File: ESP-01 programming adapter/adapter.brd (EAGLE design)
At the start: 27 x 31 mm, 9 parts

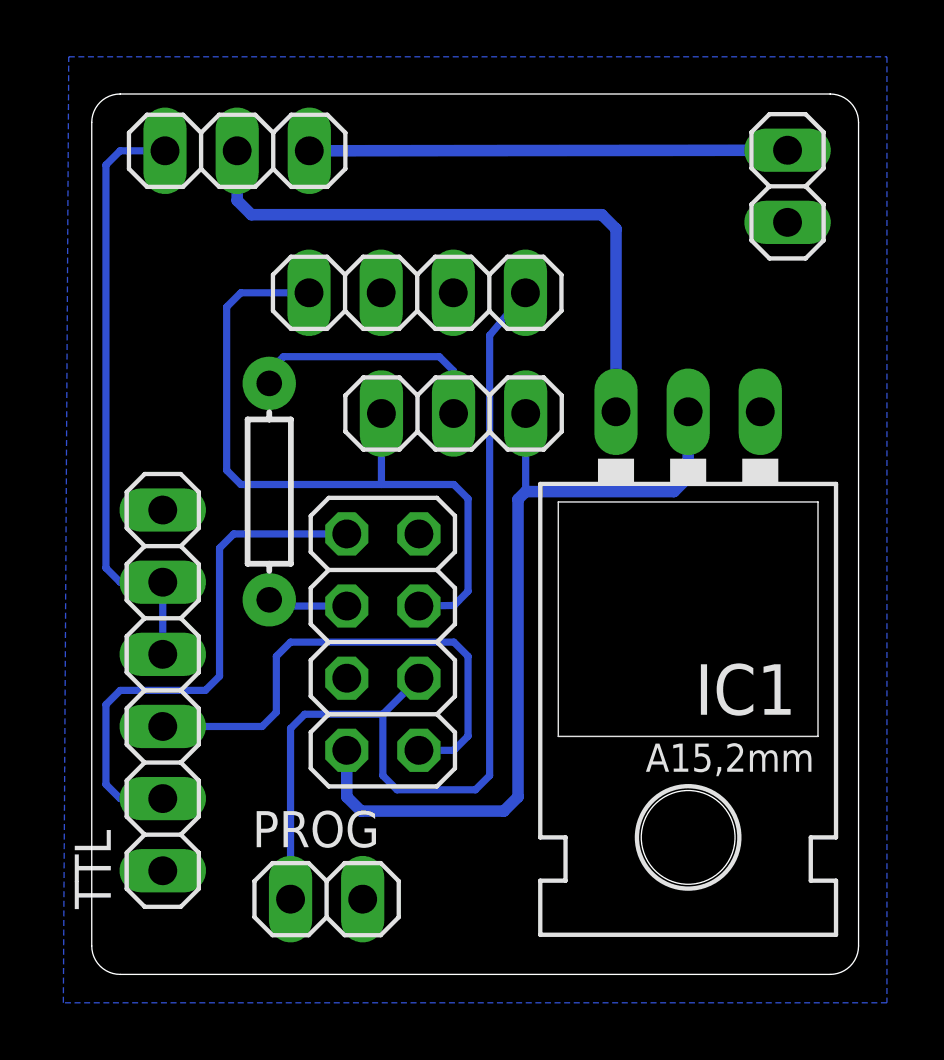
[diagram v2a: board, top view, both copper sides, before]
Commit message: CH_PD
Pin connected to GPIO00 instead of 02, so GPIO02 is free to do external
triggers.
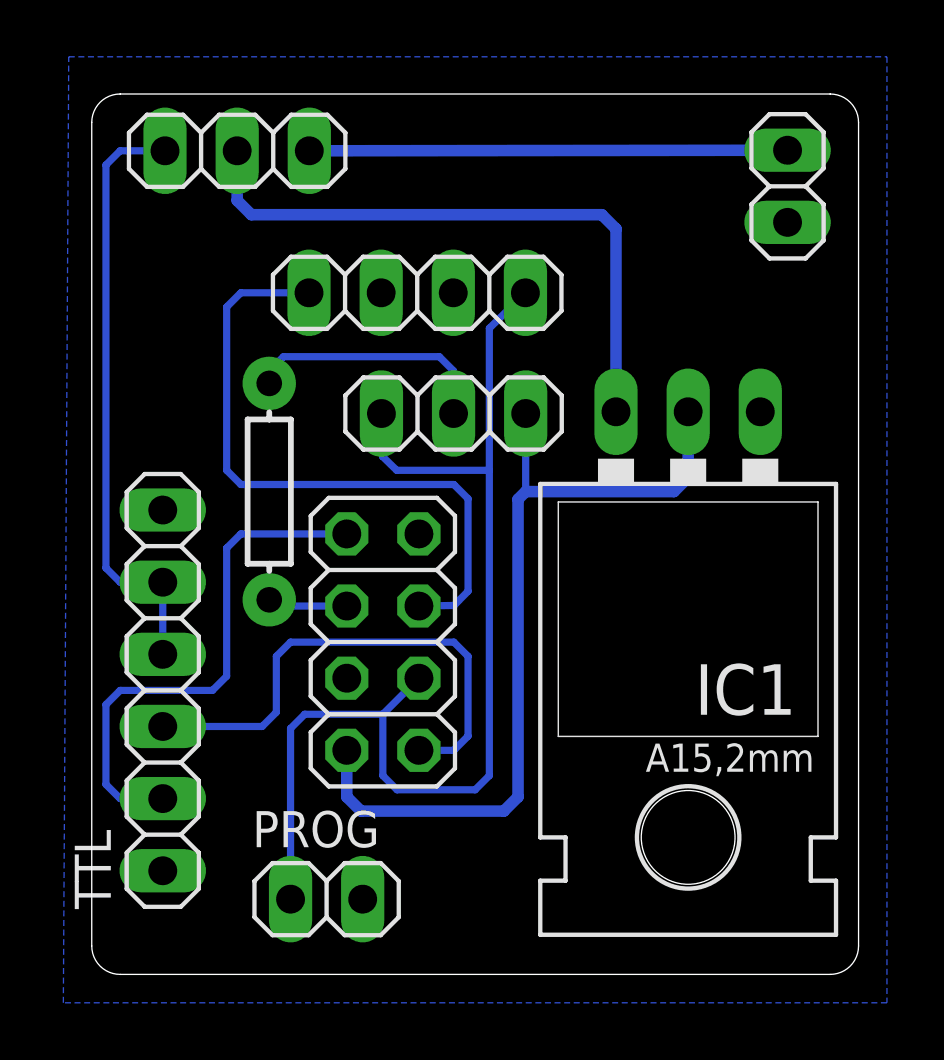
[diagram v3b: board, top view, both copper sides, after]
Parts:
- renumbered V-SEL1 to WIFI-SEL
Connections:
- removed net N$4: ESP8266-01.3, JP2.4, PROG.1
- new net N$6: ESP8266-01.3, JP2.4, PROG.1, WIFI-SEL.3
- net N$9: no longer WIFI-SEL.3
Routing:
- net N$6: track 0.00 -> 40.6 mm
- net N$4: track 35.1 -> 0.00 mm
- net N$9: track 25.5 -> 23.0 mm
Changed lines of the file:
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@@
 <attribute name="VALUE" x="6.631" y="14.968" size="1.016" layer="21" font="vector" ratio="15" rot="R90"/>
 </element>
-<element name="V-SEL1" library="pinhead" package="1X03" value="" x="12.74" y="19.75" smashed="yes" rot="R180">
+<element name="WIFI-SEL" library="pinhead" package="1X03" value="" x="12.74" y="19.75" smashed="yes" rot="R180">
 <attribute name="VALUE" x="16.55" y="22.925" size="1.27" layer="27" rot="R180"/>
 </element>
@@
 <contactref element="TTL" pad="2"/>
 <contactref element="ESP8266-01" pad="8"/>
-<wire x1="4.5" y1="10.5" x2="4.5" y2="15.01" width="0.254" layer="16"/>
-<wire x1="4.5" y1="15.01" x2="5" y2="15.51" width="0.254" layer="16"/>
-<wire x1="5" y1="15.51" x2="8.98" y2="15.51" width="0.254" layer="16"/>
-<wire x1="4.5" y1="10.5" x2="4" y2="10" width="0.254" layer="16"/>
-<wire x1="4" y1="10" x2="1" y2="10" width="0.254" layer="16"/>
+<wire x1="4.75" y1="10.5" x2="4.75" y2="15.01" width="0.254" layer="16"/>
+<wire x1="4.75" y1="15.01" x2="5.25" y2="15.51" width="0.254" layer="16"/>
+<wire x1="5.25" y1="15.51" x2="8.98" y2="15.51" width="0.254" layer="16"/>
+<wire x1="4.75" y1="10.5" x2="4.25" y2="10" width="0.254" layer="16"/>
+<wire x1="4.25" y1="10" x2="1" y2="10" width="0.254" layer="16"/>
 <wire x1="1" y1="10" x2="0.5" y2="9.5" width="0.254" layer="16"/>
 <wire x1="2.5" y1="6.19" x2="1" y2="6.19" width="0.254" layer="16"/>
@@
 <wire x1="12.75" y1="7.89" x2="13.25" y2="8.39" width="0.254" layer="16"/>
 </signal>
-<signal name="N$4">
-<contactref element="ESP8266-01" pad="3"/>
-<contactref element="PROG" pad="1"/>
-<wire x1="11.52" y1="10.43" x2="10.25" y2="9.16" width="0.254" layer="16"/>
-<wire x1="10.25" y1="9.16" x2="7.5" y2="9.16" width="0.254" layer="16"/>
-<wire x1="7.5" y1="9.16" x2="7" y2="8.66" width="0.254" layer="16"/>
-<wire x1="7" y1="8.66" x2="7" y2="2.65" width="0.254" layer="16"/>
-<contactref element="JP2" pad="4"/>
-<wire x1="15.27" y1="24" x2="14.01" y2="22.5" width="0.254" layer="16"/>
-<wire x1="14.01" y1="22.5" x2="14.01" y2="7" width="0.254" layer="16"/>
-<wire x1="14.01" y1="7" x2="13.51" y2="6.5" width="0.254" layer="16"/>
-<wire x1="13.51" y1="6.5" x2="10.75" y2="6.5" width="0.254" layer="16"/>
-<wire x1="10.75" y1="6.5" x2="10.25" y2="7" width="0.254" layer="16"/>
-<wire x1="10.25" y1="7" x2="10.25" y2="9.16" width="0.254" layer="16"/>
-</signal>
 <signal name="N$1">
 <contactref element="ESP8266-01" pad="2"/>
@@
 <wire x1="8.98" y1="6.25" x2="8.98" y2="7.89" width="0.4064" layer="16"/>
 <wire x1="15.01" y1="16.73" x2="15.28" y2="17" width="0.4064" layer="16"/>
-<contactref element="V-SEL1" pad="1"/>
+<contactref element="WIFI-SEL" pad="1"/>
 <wire x1="15.28" y1="19.75" x2="15.28" y2="17" width="0.254" layer="16"/>
 <contactref element="IC1" pad="GND"/>
@@
 <contactref element="ESP8266-01" pad="5"/>
 <contactref element="JP2" pad="1"/>
-<wire x1="10.2" y1="17.25" x2="12.75" y2="17.25" width="0.254" layer="16"/>
 <wire x1="12.75" y1="17.25" x2="13.25" y2="16.75" width="0.254" layer="16"/>
 <wire x1="13.25" y1="16.75" x2="13.25" y2="13.491403125" width="0.254" layer="16"/>
 <wire x1="13.25" y1="13.491403125" x2="12.75866875" y2="12.99148125" width="0.254" layer="16"/>
 <wire x1="12.75866875" y1="12.99148125" x2="11.52" y2="12.97" width="0.254" layer="16"/>
-<contactref element="V-SEL1" pad="3"/>
-<wire x1="10.2" y1="19.75" x2="10.2" y2="17.25" width="0.254" layer="16"/>
-<wire x1="10.2" y1="17.25" x2="5.25" y2="17.25" width="0.254" layer="16"/>
+<wire x1="12.75" y1="17.25" x2="5.25" y2="17.25" width="0.254" layer="16"/>
 <wire x1="5.25" y1="17.25" x2="4.75" y2="17.75" width="0.254" layer="16"/>
 <wire x1="4.75" y1="17.75" x2="4.75" y2="23.5" width="0.254" layer="16"/>
@@
 </signal>
 <signal name="N$10">
-<contactref element="V-SEL1" pad="2"/>
+<contactref element="WIFI-SEL" pad="2"/>
 <contactref element="R1" pad="P$2"/>
 <wire x1="6.25" y1="20.81" x2="6.25" y2="21.25" width="0.254" layer="16"/>
@@
 <wire x1="5.12" y1="27.25" x2="5.12" y2="29" width="0.4064" layer="16"/>
 </signal>
+<signal name="N$6">
+<contactref element="WIFI-SEL" pad="3"/>
+<contactref element="PROG" pad="1"/>
+<contactref element="JP2" pad="4"/>
+<contactref element="ESP8266-01" pad="3"/>
+<wire x1="11.52" y1="10.43" x2="10.25" y2="9.16" width="0.254" layer="16"/>
+<wire x1="10.25" y1="9.16" x2="10.25" y2="7" width="0.254" layer="16"/>
+<wire x1="10.25" y1="7" x2="10.75" y2="6.5" width="0.254" layer="16"/>
+<wire x1="10.75" y1="6.5" x2="13.5" y2="6.5" width="0.254" layer="16"/>
+<wire x1="13.5" y1="6.5" x2="14" y2="7" width="0.254" layer="16"/>
+<wire x1="14" y1="7" x2="14" y2="17.75" width="0.254" layer="16"/>
+<wire x1="14" y1="17.75" x2="10.73765625" y2="17.75" width="0.254" layer="16"/>
+<wire x1="10.73765625" y1="17.75" x2="10.2378125" y2="18.2375" width="0.254" layer="16"/>
+<wire x1="10.2378125" y1="18.2375" x2="10.2" y2="19.75" width="0.254" layer="16"/>
+<wire x1="15.27" y1="24" x2="14" y2="22.75" width="0.254" layer="16"/>
+<wire x1="14" y1="22.75" x2="14" y2="17.75" width="0.254" layer="16"/>
+<wire x1="7" y1="2.65" x2="7" y2="8.66" width="0.254" layer="16"/>
+<wire x1="7" y1="8.66" x2="7.5" y2="9.16" width="0.254" layer="16"/>
+<wire x1="7.5" y1="9.16" x2="10.25" y2="9.16" width="0.254" layer="16"/>
+</signal>
 </signals>
